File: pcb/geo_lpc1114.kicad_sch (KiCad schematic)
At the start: 129 parts, among them J1 CN_SWD, J10 Screw_Terminal_01x02, J11 Screw_Terminal_01x02, J12 Screw_Terminal_01x02, J13 Screw_Terminal_01x02, J14 Screw_Terminal_01x02, J15 Screw_Terminal_01x02, J16 Screw_Terminal_01x02, J17 Screw_Terminal_01x02, J18 USB_B, J19 MJ-179PH, J2 AQM1602Y-NLW-FBW, J3 GPIO_Header, J4 I2C_Header, J5 UART_Header, J6 Screw_Terminal_01x02, J7 Screw_Terminal_01x02, J8 Screw_Terminal_01x02, J9 Screw_Terminal_01x02, Q3 S8550, Q4 S8550, Q5 S8550, Q6 S8550, Q7 S8550, Q8 S8550, SW1 SW, SW2 SW, U1 LPC1114FN28-102, U10 LPC1114FDH28-102, U11 CH340N, U12 LM2940T-3.3, U4 HX711, U5 HX711, U6 HX711, U7 HX711, U8 HX711, U9 HX711, Y1 12MHz

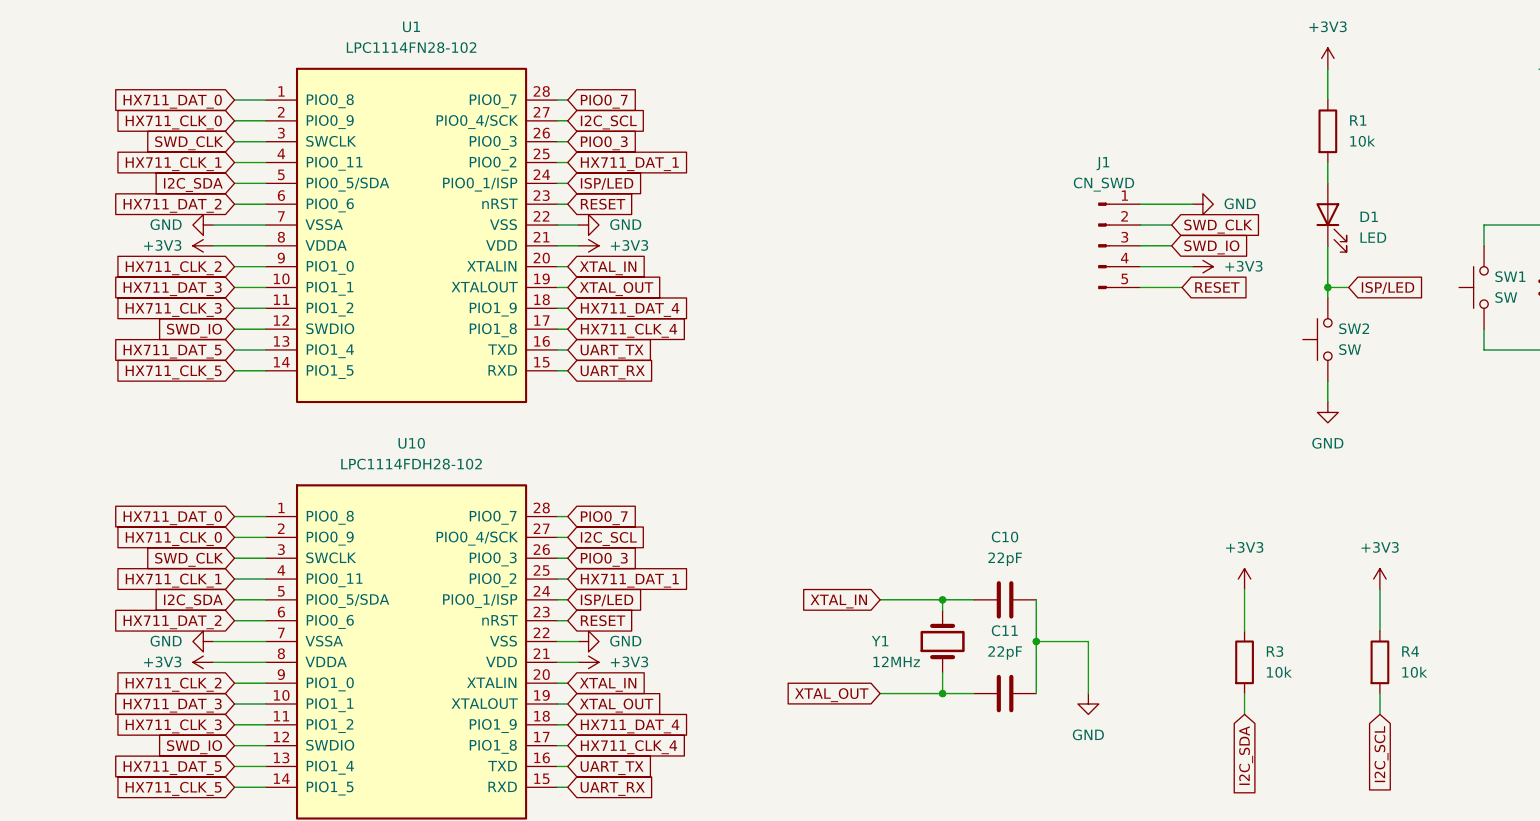
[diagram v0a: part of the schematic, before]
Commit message: move dir & Fix VDDA/VSSA pin mapping
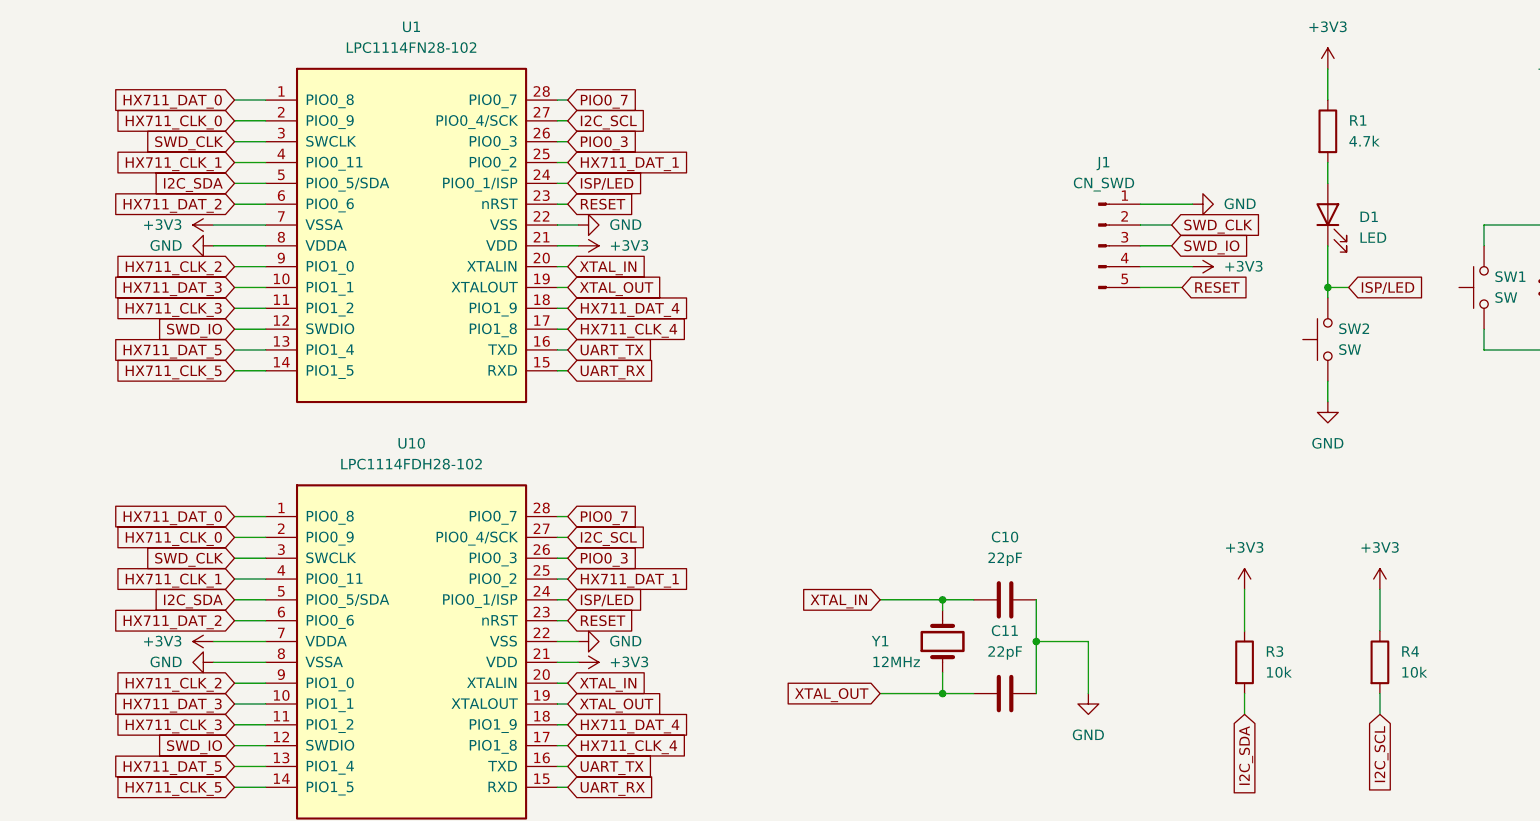
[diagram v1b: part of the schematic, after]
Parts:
- R1: value 10k -> 4.7k
- U12: footprint Package_TO_SOT_THT:TO-220F-3_Horizontal_TabDown -> Package_TO_SOT_THT:TO-220-3_Horizontal_TabDown
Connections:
- net +3V3: now also U1.7 (VSSA), U10.7 (VDDA); no longer U1.8 (VDDA), U10.8 (VDDA)
- net GND: now also U1.8 (VDDA), U10.8 (VSSA); no longer U1.7 (VSSA), U10.7 (VSSA)
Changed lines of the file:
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@@
 	(symbol
 		(lib_id "power:GND")
-		(at 49.53 43.18 270)
+		(at 49.53 45.72 270)
 		(unit 1)
 		(exclude_from_sim no)
@@
 		(fields_autoplaced yes)
 		(property "Reference" "#PWR03"
-			(at 43.18 43.18 0)
+			(at 43.18 45.72 0)
 			(effects
 				(font
@@
 		)
 		(property "Value" "GND"
-			(at 45.72 43.1799 90)
+			(at 45.72 45.7199 90)
 			(effects
 				(font
@@
 		)
 		(property "Footprint" ""
-			(at 49.53 43.18 0)
+			(at 49.53 45.72 0)
 			(effects
 				(font
@@
 		)
 		(property "Datasheet" ""
-			(at 49.53 43.18 0)
+			(at 49.53 45.72 0)
 			(effects
 				(font
@@
 		)
 		(property "Description" "Power symbol creates a global label with name \"GND\" , ground"
-			(at 49.53 43.18 0)
+			(at 49.53 45.72 0)
 			(effects
 				(font
@@
 	(symbol
 		(lib_id "power:VCC")
-		(at 49.53 45.72 90)
+		(at 49.53 43.18 90)
 		(unit 1)
 		(exclude_from_sim no)
@@
 		(fields_autoplaced yes)
 		(property "Reference" "#PWR05"
-			(at 53.34 45.72 0)
+			(at 53.34 43.18 0)
 			(effects
 				(font
@@
 		)
 		(property "Value" "+3V3"
-			(at 45.72 45.7199 90)
+			(at 45.72 43.1799 90)
 			(effects
 				(font
@@
 		)
 		(property "Footprint" ""
-			(at 49.53 45.72 0)
+			(at 49.53 43.18 0)
 			(effects
 				(font
@@
 		)
 		(property "Datasheet" ""
-			(at 49.53 45.72 0)
+			(at 49.53 43.18 0)
 			(effects
 				(font
@@
 		)
 		(property "Description" "Power symbol creates a global label with name \"VCC\""
-			(at 49.53 45.72 0)
+			(at 49.53 43.18 0)
 			(effects
 				(font
@@
 	(symbol
 		(lib_id "power:GND")
-		(at 49.53 93.98 270)
+		(at 49.53 96.52 270)
 		(unit 1)
 		(exclude_from_sim no)
@@
 		(fields_autoplaced yes)
 		(property "Reference" "#PWR053"
-			(at 43.18 93.98 0)
+			(at 43.18 96.52 0)
 			(effects
 				(font
@@
 		)
 		(property "Value" "GND"
-			(at 45.72 93.9799 90)
+			(at 45.72 96.5199 90)
 			(effects
 				(font
@@
 		)
 		(property "Footprint" ""
-			(at 49.53 93.98 0)
+			(at 49.53 96.52 0)
 			(effects
 				(font
@@
 		)
 		(property "Datasheet" ""
-			(at 49.53 93.98 0)
+			(at 49.53 96.52 0)
 			(effects
 				(font
@@
 		)
 		(property "Description" "Power symbol creates a global label with name \"GND\" , ground"
-			(at 49.53 93.98 0)
+			(at 49.53 96.52 0)
 			(effects
 				(font
@@
 	(symbol
 		(lib_id "power:VCC")
-		(at 49.53 96.52 90)
+		(at 49.53 93.98 90)
 		(unit 1)
 		(exclude_from_sim no)
@@
 		(fields_autoplaced yes)
 		(property "Reference" "#PWR054"
-			(at 53.34 96.52 0)
+			(at 53.34 93.98 0)
 			(effects
 				(font
@@
 		)
 		(property "Value" "+3V3"
-			(at 45.72 96.5199 90)
+			(at 45.72 93.9799 90)
 			(effects
 				(font
@@
 		)
 		(property "Footprint" ""
-			(at 49.53 96.52 0)
+			(at 49.53 93.98 0)
 			(effects
 				(font
@@
 		)
 		(property "Datasheet" ""
-			(at 49.53 96.52 0)
+			(at 49.53 93.98 0)
 			(effects
 				(font
@@
 		)
 		(property "Description" "Power symbol creates a global label with name \"VCC\""
-			(at 49.53 96.52 0)
+			(at 49.53 93.98 0)
 			(effects
 				(font
@@
 			)
 		)
-		(property "Value" "10k"
+		(property "Value" "4.7k"
 			(at 187.96 33.0199 0)
 			(effects
@@
 			)
 		)
-		(property "Footprint" "Package_TO_SOT_THT:TO-220F-3_Horizontal_TabDown"
+		(property "Footprint" "Package_TO_SOT_THT:TO-220-3_Horizontal_TabDown"
 			(at 444.5 46.355 0)
 			(effects

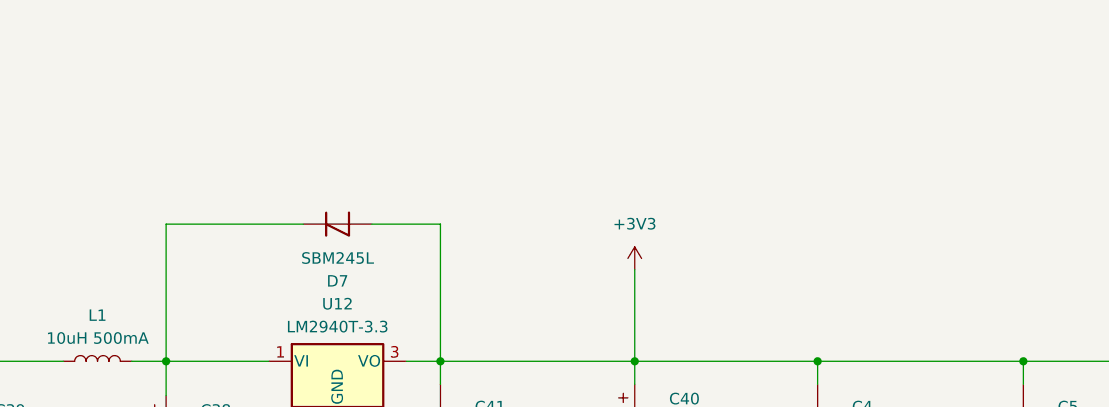
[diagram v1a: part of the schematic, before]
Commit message: AMS1117の裏面サブ実装、基盤の角丸め、ほか微修正
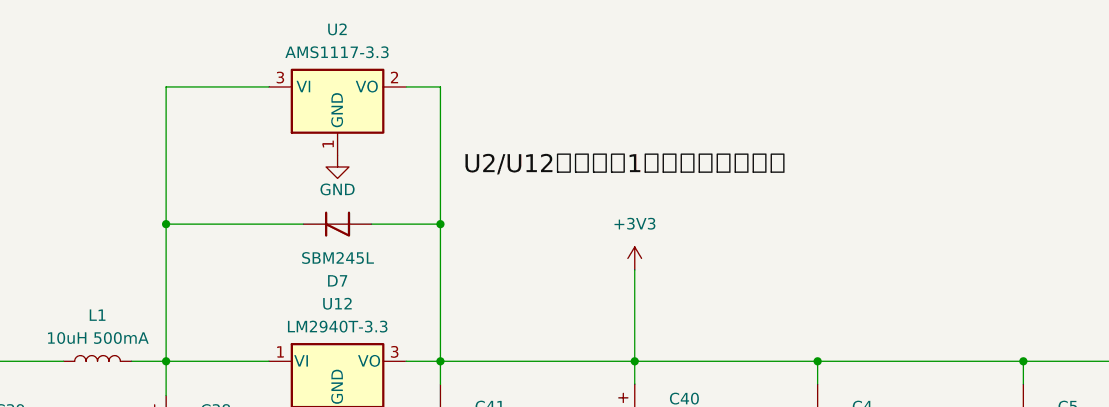
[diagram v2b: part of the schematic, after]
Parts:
- added U2: AMS1117-3.3, Package_TO_SOT_SMD:SOT-223-3_TabPin2, symbol Regulator_Linear:AMS1117-3.3
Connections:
- net +3V3: now also U2.2 (VO)
- net GND: now also U2.1 (GND)
- net at C38.1, D7.1 (K), L1.2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: now also U2.3 (VI)
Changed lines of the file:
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@@
 	)
 	(junction
+		(at 455.93 36.83)
+		(diameter 0)
+		(color 0 0 0 0)
+	)
+	(junction
 		(at 342.9 151.13)
 		(diameter 0)
@@
 	)
 	(junction
+		(at 425.45 36.83)
+		(diameter 0)
+		(color 0 0 0 0)
+	)
+	(junction
 		(at 520.7 52.07)
 		(diameter 0)
@@
 	(wire
 		(pts
+			(xy 436.88 21.59) (xy 425.45 21.59)
+		)
+		(stroke
+			(width 0)
+			(type default)
+		)
+	)
+	(wire
+		(pts
 			(xy 162.56 43.18) (xy 166.37 43.18)
 		)
@@
 	(wire
 		(pts
+			(xy 452.12 21.59) (xy 455.93 21.59)
+		)
+		(stroke
+			(width 0)
+			(type default)
+		)
+	)
+	(wire
+		(pts
 			(xy 448.31 196.85) (xy 448.31 195.58)
 		)
@@
 	(wire
 		(pts
+			(xy 455.93 21.59) (xy 455.93 36.83)
+		)
+		(stroke
+			(width 0)
+			(type default)
+		)
+	)
+	(wire
+		(pts
 			(xy 59.69 238.76) (xy 59.69 283.21)
 		)
@@
 	(wire
 		(pts
+			(xy 425.45 21.59) (xy 425.45 36.83)
+		)
+		(stroke
+			(width 0)
+			(type default)
+		)
+	)
+	(wire
+		(pts
 			(xy 77.47 262.89) (xy 74.93 262.89)
 		)
@@
 		)
 	)
+	(label "U2{slash}U12どちらか1個のみ実装する事"
+		(at 458.47 31.75 0)
+		(effects
+			(font
+				(size 2 2)
+			)
+			(justify left bottom)
+		)
+	)
 	(global_label "HX711_CLK_2"
 		(shape input)
@@
 	)
 	(symbol
+		(lib_id "Regulator_Linear:AMS1117-3.3")
+		(at 444.5 21.59 0)
+		(unit 1)
+		(exclude_from_sim no)
+		(in_bom yes)
+		(on_board yes)
+		(dnp no)
+		(fields_autoplaced yes)
+		(property "Reference" "U2"
+			(at 444.5 15.24 0)
+			(effects
+				(font
+					(size 1.27 1.27)
+				)
+			)
+		)
+		(property "Value" "AMS1117-3.3"
+			(at 444.5 17.78 0)
+			(effects
+				(font
+					(size 1.27 1.27)
+				)
+			)
+		)
+		(property "Footprint" "Package_TO_SOT_SMD:SOT-223-3_TabPin2"
+			(at 444.5 16.51 0)
+			(effects
+				(font
+					(size 1.27 1.27)
+				)
+				(hide yes)
+			)
+		)
+		(property "Datasheet" "http://www.advanced-monolithic.com/pdf/ds1117.pdf"
+			(at 447.04 27.94 0)
+			(effects
+				(font
+					(size 1.27 1.27)
+				)
+				(hide yes)
+			)
+		)
+		(property "Description" "1A Low Dropout regulator, positive, 3.3V fixed output, SOT-223"
+			(at 444.5 21.59 0)
+			(effects
+				(font
+					(size 1.27 1.27)
+				)
+				(hide yes)
+			)
+		)
+		(pin "2"
+		)
+		(pin "3"
+		)
+		(pin "1"
+		)
+		(instances
+			(project ""
+				(path "/b39a4d71-1528-41f6-8466-62558d4d31a9"
+					(reference "U2")
+					(unit 1)
+				)
+			)
+		)
+	)
+	(symbol
 		(lib_id "power:GND")
 		(at 156.21 100.33 0)
@@
 					(unit 1)
 				)
+			)
+		)
+	)
+	(symbol
+		(lib_id "power:GND")
+		(at 444.5 29.21 0)
+		(mirror y)
+		(unit 1)
+		(exclude_from_sim no)
+		(in_bom yes)
+		(on_board yes)
+		(dnp no)
+		(property "Reference" "#PWR068"
+			(at 444.5 35.56 0)
+			(effects
+				(font
+					(size 1.27 1.27)
+				)
+				(hide yes)
+			)
+		)
+		(property "Value" "GND"
+			(at 444.5 33.02 0)
+			(effects
+				(font
+					(size 1.27 1.27)
+				)
+			)
+		)
+		(property "Footprint" ""
+			(at 444.5 29.21 0)
+			(effects
+				(font
+					(size 1.27 1.27)
+				)
+				(hide yes)
+			)
+		)
+		(property "Datasheet" ""
+			(at 444.5 29.21 0)
+			(effects
+				(font
+					(size 1.27 1.27)
+				)
+				(hide yes)
+			)
+		)
+		(property "Description" "Power symbol creates a global label with name \"GND\" , ground"
+			(at 444.5 29.21 0)
+			(effects
+				(font
+					(size 1.27 1.27)
+				)
+				(hide yes)
+			)
+		)
+		(pin "1"
+		)
+		(instances
+			(project "geo_lpc1114"
+				(path "/b39a4d71-1528-41f6-8466-62558d4d31a9"
+					(reference "#PWR068")
+					(unit 1)
+				)
